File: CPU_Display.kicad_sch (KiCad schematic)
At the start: 1 part

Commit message: Some DP and power work
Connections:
- net iGPU_DDI1_TX2-: now reaches JCPU1.A23 (DDI1_TXN_2)
- net iGPU_DDI1_AUX+: now reaches JCPU1.B13 (DDI1_AUXP)
- net iGPU_DDI1_TX2+: now reaches JCPU1.B23 (DDI1_TXP_2)
- net iGPU_DDI1_AUX-: now reaches JCPU1.C13 (DDI1_AUXN)
- net iGPU_DDI1_TX0+: now reaches JCPU1.C21 (DDI1_TXP_0)
- net iGPU_DDI1_TX3+: now reaches JCPU1.C23 (DDI1_TXP_3)
- net iGPU_DDI1_TX0-: now reaches JCPU1.D21 (DDI1_TXN_0)
- net iGPU_DDI1_TX1+: now reaches JCPU1.D22 (DDI1_TXP_1)
- net iGPU_DDI1_TX3-: now reaches JCPU1.D23 (DDI1_TXN_3)
- net iGPU_DDI1_TX1-: now reaches JCPU1.E22 (DDI1_TXN_1)
- net CPU_DisplayAudio_SDO: now reaches JCPU1.U1 (PROC_AUDIO_SDO)
- net CPU_DisplayAudio_SDI: now reaches JCPU1.V2 (PROC_AUDIO_SDI)
- net CPU_DisplayAudio_CLK: now reaches JCPU1.V3 (PROC_AUDIO_CLK)

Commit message: More DP
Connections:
- net iGPU_DDI2_AUX+: now reaches JCPU1.A12 (DDI2_AUXP)
- net iGPU_DDI3_TX0-: now reaches JCPU1.A14 (DDI3_TXN_0)
- net iGPU_DDI3_TX2-: now reaches JCPU1.A16 (DDI3_TXN_2)
- net iGPU_DDI2_TX0-: now reaches JCPU1.A18 (DDI2_TXN_0)
- net iGPU_DDI3_AUX+: now reaches JCPU1.B11 (DDI3_AUXP)
- net iGPU_DDI2_AUX-: now reaches JCPU1.B12 (DDI2_AUXN)
- net iGPU_DDI3_TX0+: now reaches JCPU1.B14 (DDI3_TXP_0)
- net iGPU_DDI3_TX1-: now reaches JCPU1.B15 (DDI3_TXN_1)
- net iGPU_DDI3_TX2+: now reaches JCPU1.B16 (DDI3_TXP_2)
- net iGPU_DDI3_TX3-: now reaches JCPU1.B17 (DDI3_TXN_3)
- net iGPU_DDI2_TX0+: now reaches JCPU1.B18 (DDI2_TXP_0)
- net iGPU_DDI3_AUX-: now reaches JCPU1.C11 (DDI3_AUXN)
- net iGPU_DDI3_TX1+: now reaches JCPU1.C15 (DDI3_TXP_1)
- net iGPU_DDI3_TX3+: now reaches JCPU1.C17 (DDI3_TXP_3)
- net iGPU_DDI2_TX2+: now reaches JCPU1.C19 (DDI2_TXP_2)
- net iGPU_DDI2_TX1+: now reaches JCPU1.D18 (DDI2_TXP_1)
- net iGPU_DDI2_TX2-: now reaches JCPU1.D19 (DDI2_TXN_2)
- net iGPU_DDI2_TX3+: now reaches JCPU1.D20 (DDI2_TXP_3)
- net iGPU_DDI2_TX1-: now reaches JCPU1.E18 (DDI2_TXN_1)
- net iGPU_DDI2_TX3-: now reaches JCPU1.E20 (DDI2_TXN_3)

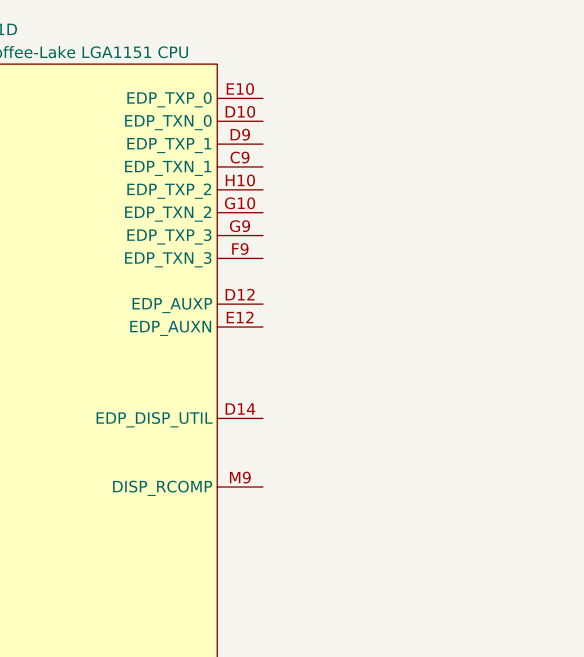
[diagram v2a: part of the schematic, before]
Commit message: partially added eDP + rearranged other display stuff
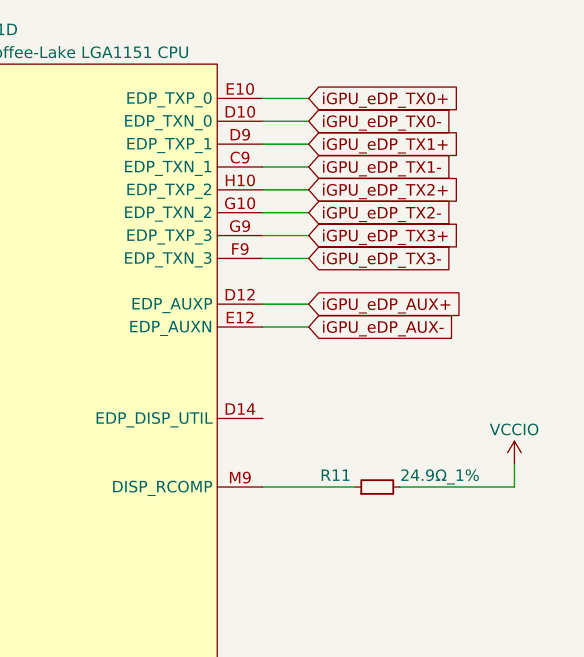
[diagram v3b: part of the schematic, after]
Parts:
- added R11: 24.9Ω_1%, Resistor_SMD:R_0402_1005Metric, symbol Device:R_Small
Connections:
- net iGPU_eDP_TX1-: now reaches JCPU1.C9 (EDP_TXN_1)
- net iGPU_eDP_TX0-: now reaches JCPU1.D10 (EDP_TXN_0)
- net iGPU_eDP_AUX+: now reaches JCPU1.D12 (EDP_AUXP)
- net iGPU_eDP_TX1+: now reaches JCPU1.D9 (EDP_TXP_1)
- net iGPU_eDP_TX0+: now reaches JCPU1.E10 (EDP_TXP_0)
- net iGPU_eDP_AUX-: now reaches JCPU1.E12 (EDP_AUXN)
- net iGPU_eDP_TX3-: now reaches JCPU1.F9 (EDP_TXN_3)
- net iGPU_eDP_TX2-: now reaches JCPU1.G10 (EDP_TXN_2)
- net iGPU_eDP_TX3+: now reaches JCPU1.G9 (EDP_TXP_3)
- net iGPU_eDP_TX2+: now reaches JCPU1.H10 (EDP_TXP_2)
- net at JCPU1.M9 (DISP_RCOMP): now also R11.1
- new net VCCIO: R11.2

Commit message: Added PCH PCIe rootport/bifurcation notes
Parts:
- added TP1: eDP-pwm-but-from-CPU?, TestPoint:TestPoint_Pad_D2.0mm, symbol Connector:TestPoint
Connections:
- net at JCPU1.D14 (EDP_DISP_UTIL): now also TP1.1
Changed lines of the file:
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@@
 	(wire
 		(pts
+			(xy 179.07 83.82) (xy 212.09 83.82)
+		)
+		(stroke
+			(width 0)
+			(type default)
+		)
+	)
+	(wire
+		(pts
 			(xy 189.23 91.44) (xy 179.07 91.44)
 		)
@@
 					(unit 1)
 				)
+			)
+		)
+	)
+	(symbol
+		(lib_id "Connector:TestPoint")
+		(at 212.09 83.82 270)
+		(unit 1)
+		(exclude_from_sim no)
+		(in_bom yes)
+		(on_board yes)
+		(dnp no)
+		(fields_autoplaced yes)
+		(property "Reference" "TP1"
+			(at 217.17 82.5499 90)
+			(effects
+				(font
+					(size 1.27 1.27)
+				)
+				(justify left)
+			)
+		)
+		(property "Value" "eDP-pwm-but-from-CPU?"
+			(at 217.17 85.0899 90)
+			(effects
+				(font
+					(size 1.27 1.27)
+				)
+				(justify left)
+			)
+		)
+		(property "Footprint" "TestPoint:TestPoint_Pad_D2.0mm"
+			(at 212.09 88.9 0)
+			(effects
+				(font
+					(size 1.27 1.27)
+				)
+				(hide yes)
+			)
+		)
+		(property "Datasheet" "~"
+			(at 212.09 88.9 0)
+			(effects
+				(font
+					(size 1.27 1.27)
+				)
+				(hide yes)
+			)
+		)
+		(property "Description" "test point"
+			(at 212.09 83.82 0)
+			(effects
+				(font
+					(size 1.27 1.27)
+				)
+				(hide yes)
+			)
+		)
+		(pin "1"
+		)
+		(instances
+			(project ""
+				(path "/4bc771b8-eb19-46d0-8798-27231a7c6e83/f32a0628-54c2-4f5a-8fa3-eb09958bebe4"
+					(reference "TP1")
+					(unit 1)
+				)

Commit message: stroopwafel.exe
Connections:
- net CPU_DisplayAudio_CLK: no longer JCPU1.V3 (PROC_AUDIO_CLK)
- net CPU_DisplayAudio_SDI: no longer JCPU1.V2 (PROC_AUDIO_SDI)
- net CPU_DisplayAudio_SDO: no longer JCPU1.U1 (PROC_AUDIO_SDO)
- net iGPU_DDI1_AUX+: no longer JCPU1.B13 (DDI1_AUXP)
- net iGPU_DDI1_AUX-: no longer JCPU1.C13 (DDI1_AUXN)
- net iGPU_DDI1_TX0+: no longer JCPU1.C21 (DDI1_TXP_0)
- net iGPU_DDI1_TX0-: no longer JCPU1.D21 (DDI1_TXN_0)
- net iGPU_DDI1_TX1+: no longer JCPU1.D22 (DDI1_TXP_1)
- net iGPU_DDI1_TX1-: no longer JCPU1.E22 (DDI1_TXN_1)
- net iGPU_DDI1_TX2+: no longer JCPU1.B23 (DDI1_TXP_2)
- net iGPU_DDI1_TX2-: no longer JCPU1.A23 (DDI1_TXN_2)
- net iGPU_DDI1_TX3+: no longer JCPU1.C23 (DDI1_TXP_3)
- net iGPU_DDI1_TX3-: no longer JCPU1.D23 (DDI1_TXN_3)
- net iGPU_DDI2_AUX+: no longer JCPU1.A12 (DDI2_AUXP)
- net iGPU_DDI2_AUX-: no longer JCPU1.B12 (DDI2_AUXN)
- net iGPU_DDI2_TX0+: no longer JCPU1.B18 (DDI2_TXP_0)
- net iGPU_DDI2_TX0-: no longer JCPU1.A18 (DDI2_TXN_0)
- net iGPU_DDI2_TX1+: no longer JCPU1.D18 (DDI2_TXP_1)
- net iGPU_DDI2_TX1-: no longer JCPU1.E18 (DDI2_TXN_1)
- net iGPU_DDI2_TX2+: no longer JCPU1.C19 (DDI2_TXP_2)
- net iGPU_DDI2_TX2-: no longer JCPU1.D19 (DDI2_TXN_2)
- net iGPU_DDI2_TX3+: no longer JCPU1.D20 (DDI2_TXP_3)
- net iGPU_DDI2_TX3-: no longer JCPU1.E20 (DDI2_TXN_3)
- net iGPU_DDI3_AUX+: no longer JCPU1.B11 (DDI3_AUXP)
- net iGPU_DDI3_AUX-: no longer JCPU1.C11 (DDI3_AUXN)
- net iGPU_DDI3_TX0+: no longer JCPU1.B14 (DDI3_TXP_0)
- net iGPU_DDI3_TX0-: no longer JCPU1.A14 (DDI3_TXN_0)
- net iGPU_DDI3_TX1+: no longer JCPU1.C15 (DDI3_TXP_1)
- net iGPU_DDI3_TX1-: no longer JCPU1.B15 (DDI3_TXN_1)
- net iGPU_DDI3_TX2+: no longer JCPU1.B16 (DDI3_TXP_2)
- net iGPU_DDI3_TX2-: no longer JCPU1.A16 (DDI3_TXN_2)
- net iGPU_DDI3_TX3+: no longer JCPU1.C17 (DDI3_TXP_3)
- net iGPU_DDI3_TX3-: no longer JCPU1.B17 (DDI3_TXN_3)
- net iGPU_eDP_AUX+: no longer JCPU1.D12 (EDP_AUXP)
- net iGPU_eDP_AUX-: no longer JCPU1.E12 (EDP_AUXN)
- net iGPU_eDP_TX0+: no longer JCPU1.E10 (EDP_TXP_0)
- net iGPU_eDP_TX0-: no longer JCPU1.D10 (EDP_TXN_0)
- net iGPU_eDP_TX1+: no longer JCPU1.D9 (EDP_TXP_1)
- net iGPU_eDP_TX1-: no longer JCPU1.C9 (EDP_TXN_1)
- net iGPU_eDP_TX2+: no longer JCPU1.H10 (EDP_TXP_2)
- net iGPU_eDP_TX2-: no longer JCPU1.G10 (EDP_TXN_2)
- net iGPU_eDP_TX3+: no longer JCPU1.G9 (EDP_TXP_3)
- net iGPU_eDP_TX3-: no longer JCPU1.F9 (EDP_TXN_3)
- net at TP1.1: no longer JCPU1.D14 (EDP_DISP_UTIL)
- net at R11.1: no longer JCPU1.M9 (DISP_RCOMP)
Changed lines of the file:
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@@
 		(lib_id "A-my-stuff:Intel_CFL_1151")
 		(at 148.59 138.43 0)
-		(unit 4)
+		(unit 1)
 		(exclude_from_sim no)
 		(in_bom yes)
@@
 		)
 		(pin "J5"
-		)
-		(instances
-			(project ""
-				(path "/4bc771b8-eb19-46d0-8798-27231a7c6e83/061fe2d6-87c2-48c2-90bb-0928700512fc"
-					(reference "JCPU1")
-					(unit 4)
-				)
-				(path "/4bc771b8-eb19-46d0-8798-27231a7c6e83/f32a0628-54c2-4f5a-8fa3-eb09958bebe4"
-					(reference "JCPU1")
-					(unit 4)
-				)
-			)
 		)
 	)
@@
 		(pin "1"
 		)
-		(instances
-			(project ""
-				(path "/4bc771b8-eb19-46d0-8798-27231a7c6e83/f32a0628-54c2-4f5a-8fa3-eb09958bebe4"
-					(reference "TP1")
-					(unit 1)
-				)
-			)
-		)
 	)

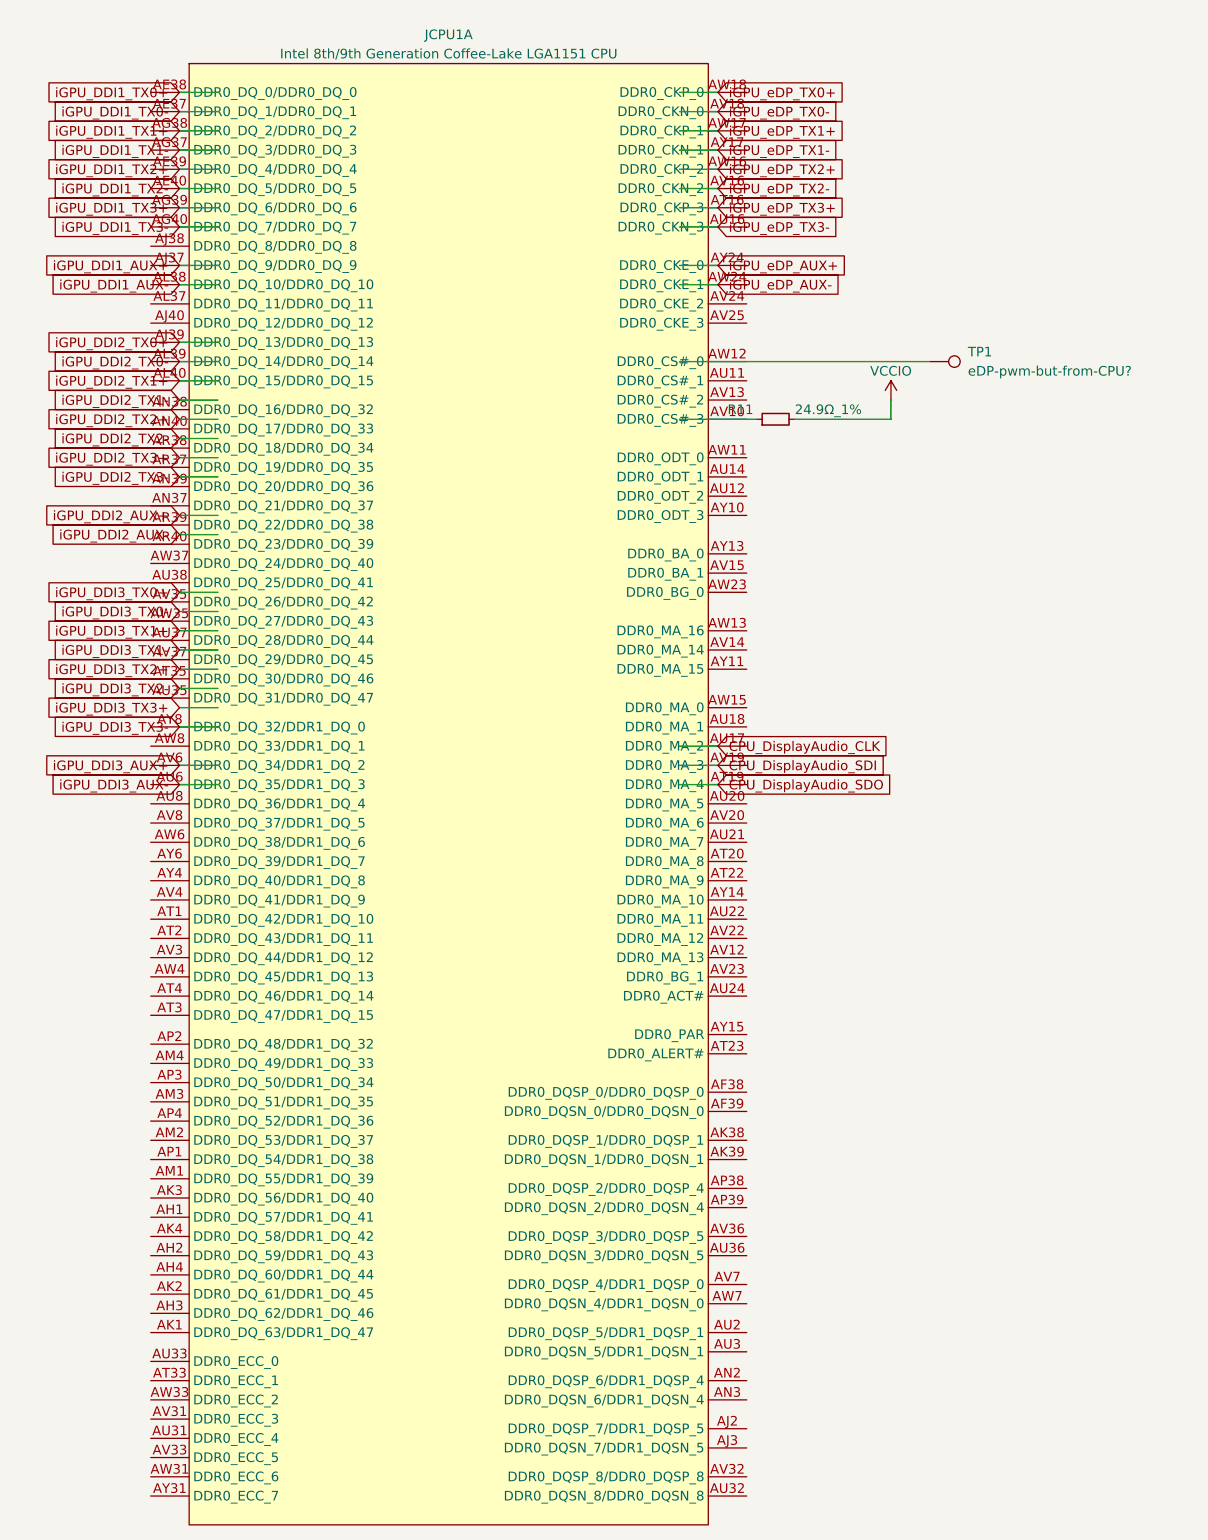
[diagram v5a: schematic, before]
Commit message: Fixed entire schematic being broken
somehow every symbol with index 1 broke and updating the pcb stopped working. how does that even happen. oh well it's fixed now
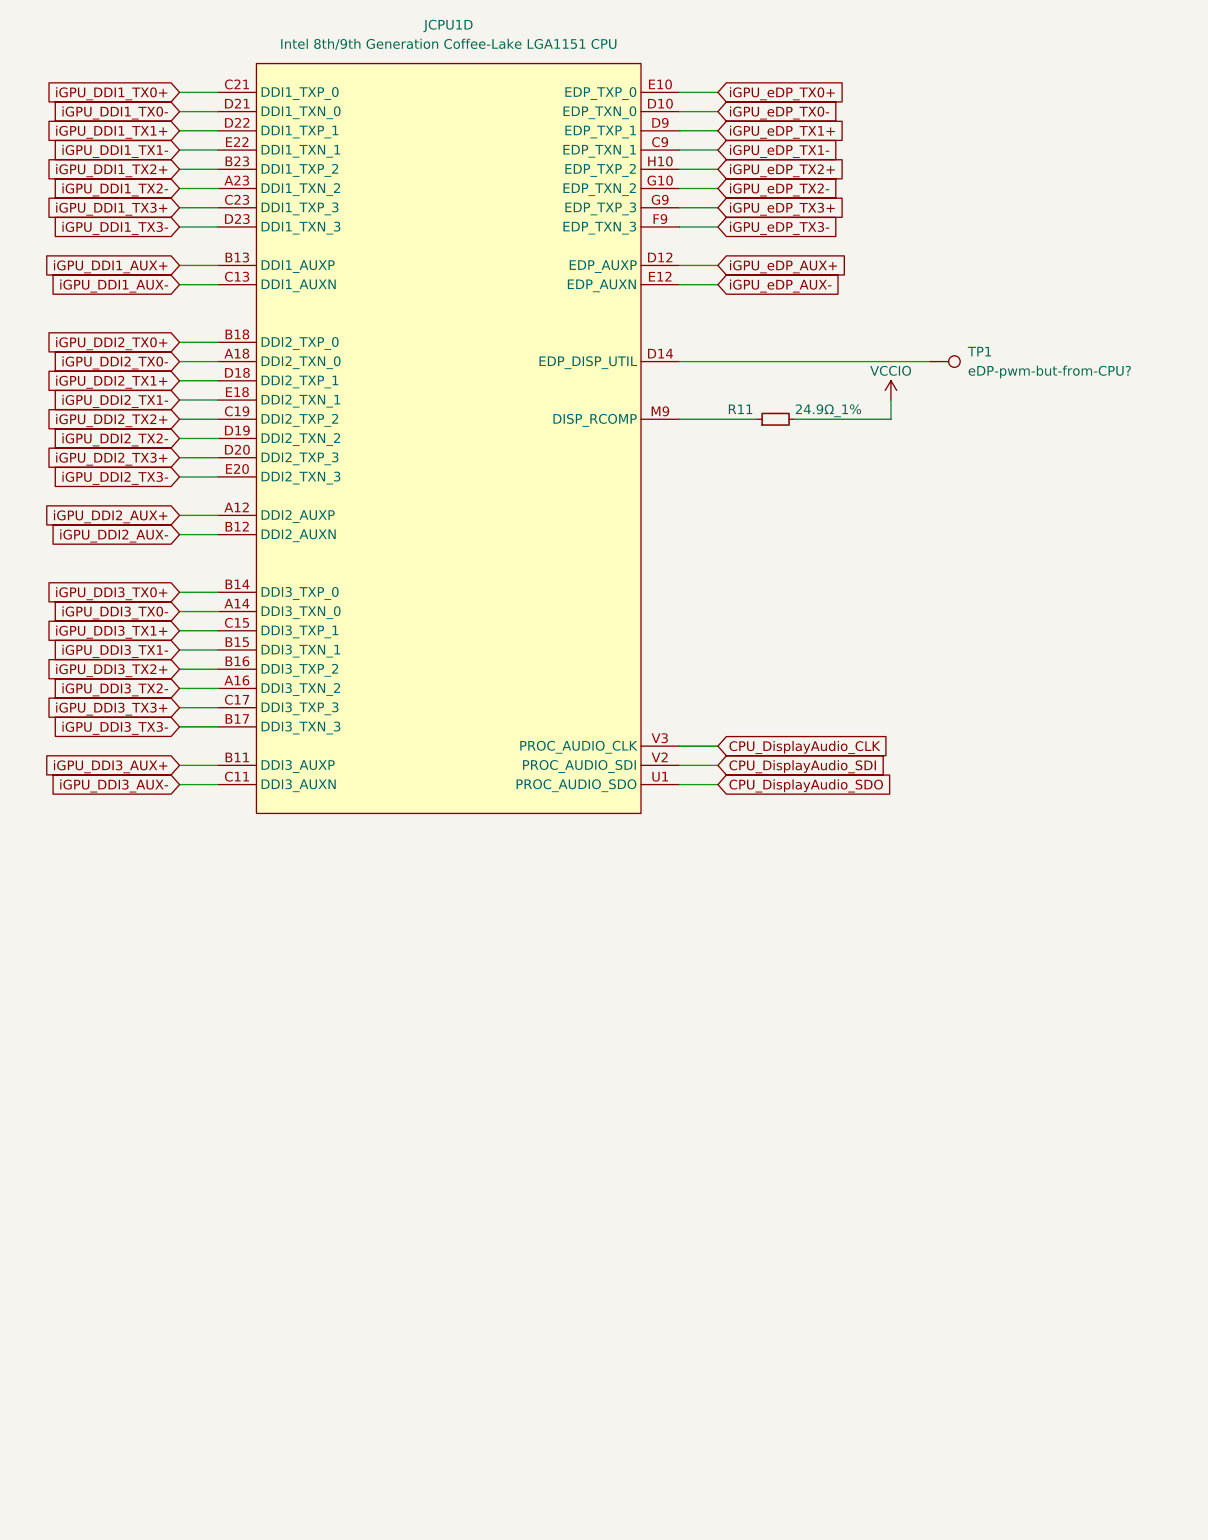
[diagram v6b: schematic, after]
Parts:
- removed JCPU1: Intel 8th/9th Generation Coffee-Lake LGA1151 CPU, A-my-stuff:LGA-1151_L47.1-W42.5-P0.91_PE115127-4041-01H, symbol A-my-stuff:Intel_CFL_1151
- added JCPU1: Intel 8th/9th Generation Coffee-Lake LGA1151 CPU, A-my-stuff:LGA-1151_L47.1-W42.5-P0.91_PE115127-4041-01H, symbol A-my-stuff:Intel_CFL_1151
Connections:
- net CPU_DisplayAudio_CLK: now also JCPU1.V3 (PROC_AUDIO_CLK)
- net CPU_DisplayAudio_SDI: now also JCPU1.V2 (PROC_AUDIO_SDI)
- net CPU_DisplayAudio_SDO: now also JCPU1.U1 (PROC_AUDIO_SDO)
- net iGPU_DDI1_AUX+: now also JCPU1.B13 (DDI1_AUXP)
- net iGPU_DDI1_AUX-: now also JCPU1.C13 (DDI1_AUXN)
- net iGPU_DDI1_TX0+: now also JCPU1.C21 (DDI1_TXP_0)
- net iGPU_DDI1_TX0-: now also JCPU1.D21 (DDI1_TXN_0)
- net iGPU_DDI1_TX1+: now also JCPU1.D22 (DDI1_TXP_1)
- net iGPU_DDI1_TX1-: now also JCPU1.E22 (DDI1_TXN_1)
- net iGPU_DDI1_TX2+: now also JCPU1.B23 (DDI1_TXP_2)
- net iGPU_DDI1_TX2-: now also JCPU1.A23 (DDI1_TXN_2)
- net iGPU_DDI1_TX3+: now also JCPU1.C23 (DDI1_TXP_3)
- net iGPU_DDI1_TX3-: now also JCPU1.D23 (DDI1_TXN_3)
- net iGPU_DDI2_AUX+: now also JCPU1.A12 (DDI2_AUXP)
- net iGPU_DDI2_AUX-: now also JCPU1.B12 (DDI2_AUXN)
- net iGPU_DDI2_TX0+: now also JCPU1.B18 (DDI2_TXP_0)
- net iGPU_DDI2_TX0-: now also JCPU1.A18 (DDI2_TXN_0)
- net iGPU_DDI2_TX1+: now also JCPU1.D18 (DDI2_TXP_1)
- net iGPU_DDI2_TX1-: now also JCPU1.E18 (DDI2_TXN_1)
- net iGPU_DDI2_TX2+: now also JCPU1.C19 (DDI2_TXP_2)
- net iGPU_DDI2_TX2-: now also JCPU1.D19 (DDI2_TXN_2)
- net iGPU_DDI2_TX3+: now also JCPU1.D20 (DDI2_TXP_3)
- net iGPU_DDI2_TX3-: now also JCPU1.E20 (DDI2_TXN_3)
- net iGPU_DDI3_AUX+: now also JCPU1.B11 (DDI3_AUXP)
- net iGPU_DDI3_AUX-: now also JCPU1.C11 (DDI3_AUXN)
- net iGPU_DDI3_TX0+: now also JCPU1.B14 (DDI3_TXP_0)
- net iGPU_DDI3_TX0-: now also JCPU1.A14 (DDI3_TXN_0)
- net iGPU_DDI3_TX1+: now also JCPU1.C15 (DDI3_TXP_1)
- net iGPU_DDI3_TX1-: now also JCPU1.B15 (DDI3_TXN_1)
- net iGPU_DDI3_TX2+: now also JCPU1.B16 (DDI3_TXP_2)
- net iGPU_DDI3_TX2-: now also JCPU1.A16 (DDI3_TXN_2)
- net iGPU_DDI3_TX3+: now also JCPU1.C17 (DDI3_TXP_3)
- net iGPU_DDI3_TX3-: now also JCPU1.B17 (DDI3_TXN_3)
- net iGPU_eDP_AUX+: now also JCPU1.D12 (EDP_AUXP)
- net iGPU_eDP_AUX-: now also JCPU1.E12 (EDP_AUXN)
- net iGPU_eDP_TX0+: now also JCPU1.E10 (EDP_TXP_0)
- net iGPU_eDP_TX0-: now also JCPU1.D10 (EDP_TXN_0)
- net iGPU_eDP_TX1+: now also JCPU1.D9 (EDP_TXP_1)
- net iGPU_eDP_TX1-: now also JCPU1.C9 (EDP_TXN_1)
- net iGPU_eDP_TX2+: now also JCPU1.H10 (EDP_TXP_2)
- net iGPU_eDP_TX2-: now also JCPU1.G10 (EDP_TXN_2)
- net iGPU_eDP_TX3+: now also JCPU1.G9 (EDP_TXP_3)
- net iGPU_eDP_TX3-: now also JCPU1.F9 (EDP_TXN_3)
- net at R11.1: now also JCPU1.M9 (DISP_RCOMP)
- net at TP1.1: now also JCPU1.D14 (EDP_DISP_UTIL)

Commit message: implemented some misc cpu signals
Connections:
- net VCCIO: now also R11.1; no longer R11.2
- net at JCPU1.M9 (DISP_RCOMP): now also R11.2; no longer R11.1
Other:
- moved on the sheet: R11
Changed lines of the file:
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@@
 	(symbol
 		(lib_id "Device:R_Small")
-		(at 191.77 91.44 90)
+		(at 191.77 91.44 270)
+		(mirror x)
 		(unit 1)
 		(exclude_from_sim no)
@@
 		(dnp no)
 		(property "Reference" "R11"
-			(at 185.42 90.17 90)
+			(at 198.12 90.17 90)
 			(effects
 				(font
@@
 		)
 		(property "Value" "24.9Ω_1%"
-			(at 194.31 90.17 90)
+			(at 189.23 90.17 90)
 			(effects
 				(font
